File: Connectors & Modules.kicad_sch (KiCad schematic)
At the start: 1 part, among them M1 Xbee_MOdule

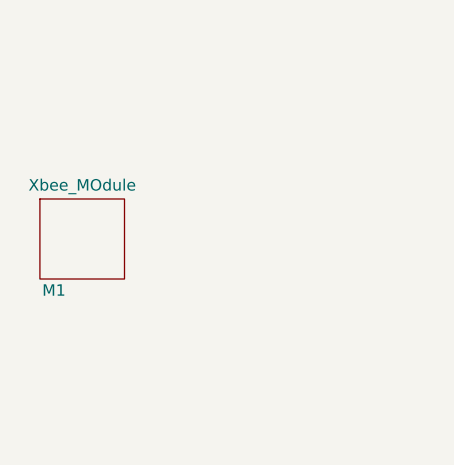
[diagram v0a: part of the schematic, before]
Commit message: Connectors Added
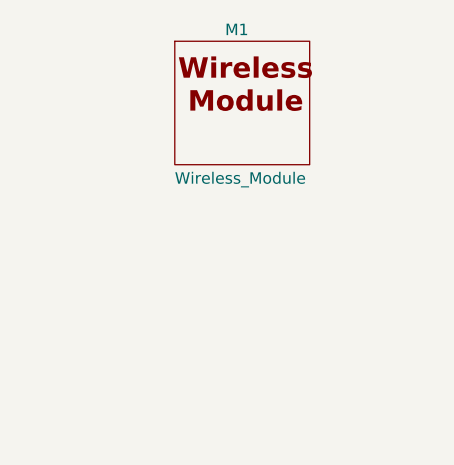
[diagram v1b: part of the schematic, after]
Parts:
- removed M1: Xbee_MOdule, LOGSUN:LGS-KC-Zbee_Mod, symbol LOGSUN:Xbee_MOD
- added M1: Wireless_Module, symbol LOGSUN:Wireless_MOD
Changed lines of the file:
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@@
+	)
+	(symbol
+		(lib_id "LOGSUN:Wireless_MOD")
+		(at 259.08 34.29 0)
+		(unit 1)
+		(exclude_from_sim no)
+		(in_bom yes)
+		(on_board yes)
+		(dnp no)
+		(property "Reference" "M1"
+			(at 258.572 24.892 0)
+			(effects
+				(font
+					(size 1.27 1.27)
+				)
+				(justify left)
+			)
+		)
+		(property "Value" "Wireless_Module"
+			(at 252.984 41.402 0)
+			(effects
+				(font
+					(size 1.27 1.27)
+				)
+				(justify left)
+			)
+		)
+		(property "Footprint" ""
+			(at 259.08 34.29 0)
+			(effects
+				(font
+					(size 1.27 1.27)
+				)
+				(hide yes)
+			)
+		)
+		(property "Datasheet" ""
+			(at 259.08 34.29 0)
+			(effects
+				(font
+					(size 1.27 1.27)
+				)
+				(hide yes)
+			)
+		)
+		(property "Description" ""
+			(at 259.08 34.29 0)
+			(effects
+				(font
+					(size 1.27 1.27)
+				)
+				(hide yes)
+			)
+		)
+		(instances
+			(project ""
+				(path "/99e6c4b3-8320-4218-aa5a-41657e7e07c6/0277d16f-7bc8-4de9-be5c-c06802e62271"
+					(reference "M1")
+					(unit 1)
+				)
+			)
+		)
 	)
 	(symbol
@@
 					(unit 1)
 				)
-			)
-		)
-	)
-	(symbol
-		(lib_id "LOGSUN:Xbee_MOD")
-		(at 241.3 46.99 0)
-		(unit 1)
-		(exclude_from_sim no)
-		(in_bom yes)
-		(on_board yes)
-		(dnp no)
-		(property "Reference" "M1"
-			(at 238.252 53.848 0)
-			(effects
-				(font
-					(size 1.27 1.27)
-				)
-				(justify left)
-			)
-		)
-		(property "Value" "Xbee_MOdule"
-			(at 236.728 42.164 0)
-			(effects
-				(font
-					(size 1.27 1.27)
-				)
-				(justify left)
-			)
-		)
-		(property "Footprint" "LOGSUN:LGS-KC-Zbee_Mod"
-			(at 241.3 46.99 0)
-			(effects
-				(font
-					(size 1.27 1.27)
-				)
-				(hide yes)
-			)
-		)
-		(property "Datasheet" ""
-			(at 241.3 46.99 0)
-			(effects
-				(font
-					(size 1.27 1.27)
-				)
-				(hide yes)
-			)
-		)
-		(property "Description" ""
-			(at 241.3 46.99 0)
-			(effects
-				(font
-					(size 1.27 1.27)
-				)
-				(hide yes)
-			)
-		)
-		(instances
-			(project ""
-				(path "/99e6c4b3-8320-4218-aa5a-41657e7e07c6/0277d16f-7bc8-4de9-be5c-c06802e62271"
-					(reference "M1")
-					(unit 1)
-				)

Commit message: Schematic Completed, Footprints Assigned
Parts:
- added J11, J12: Conn_01x03_Pin, Connector_JST:JST_EH_B3B-EH-A_1x03_P2.50mm_Vertical, symbol Connector:Conn_01x03_Pin
- added J13: I2C, Connector_JST:JST_EH_B4B-EH-A_1x04_P2.50mm_Vertical, symbol Connector:Conn_01x04_Pin
- added J14: UART, Connector_JST:JST_EH_B4B-EH-A_1x04_P2.50mm_Vertical, symbol Connector:Conn_01x04_Pin
- added J15: RGB, Connector_JST:JST_EH_B5B-EH-A_1x05_P2.50mm_Vertical, symbol Connector:Conn_01x05_Pin
- added J16: POT, Connector_JST:JST_EH_B5B-EH-A_1x05_P2.50mm_Vertical, symbol Connector:Conn_01x05_Pin
- added SV5: GP1, LOGSUN:LGS-KC-ML10-CONTROLLER, symbol LOGSUN:LGS-KC-ML10-CONTROLLER
- added SV6: GP2, LOGSUN:LGS-KC-ML10-CONTROLLER, symbol LOGSUN:LGS-KC-ML10-CONTROLLER
- added SV7: UEXT, LOGSUN:LGS-KC-ML10-CONTROLLER, symbol LOGSUN:LGS-KC-ML10-CONTROLLER
- M1: footprint (none) -> LOGSUN:LGS-KC-Wireless_Mod
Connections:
- new net +5V: J11.1 (Pin_1), J12.1 (Pin_1), J13.1 (Pin_1), J14.1 (Pin_1), SV5.1, SV6.1, SV7.1
- new net GND: J11.3 (Pin_3), J12.3 (Pin_3), J13.4 (Pin_4), J14.4 (Pin_4), SV5.2, SV6.2, SV7.2
- new net IO00: SV5.3
- new net IO02: SV5.5
- new net IO04: SV5.6
- new net IO05: SV7.10
- new net IO12: SV5.8
- new net IO13: SV5.7
- new net IO14: SV5.9
- new net IO15: SV5.4
- new net IO16: J14.3 (Pin_3), SV7.4
- new net IO17: J14.2 (Pin_2), SV7.3
- new net IO18: SV7.9
- new net IO19: SV7.7
- new net IO21: J13.3 (Pin_3), SV7.6
- new net IO22: J13.2 (Pin_2), SV7.5
- new net IO23: SV7.8
- new net IO25: SV6.9
- new net IO26: SV6.10
- new net IO27: SV5.10
- new net IO32: J12.2 (Pin_2), SV6.7
- new net IO33: J11.2 (Pin_2), SV6.8
- new net IO34: J16.4 (Pin_4), SV6.5
- new net IO35: SV6.6
- new net IO36: J16.3 (Pin_3), SV6.3
- new net IO39: J16.2 (Pin_2), SV6.4
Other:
- moved on the sheet: M1

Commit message: Bar LED Resistors Added & Mounting holes added
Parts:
- added H1, H2, H3, H4: MountingHole, MountingHole:MountingHole_3.2mm_M3_Pad_Via, symbol Mechanical:MountingHole

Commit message: Symbol and footprint library exported
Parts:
- H1, H2, H3, H4: symbol Mechanical:MountingHole -> ESP32_Xbee_LoRa:MountingHole
- J11, J12: symbol Connector:Conn_01x03_Pin -> ESP32_Xbee_LoRa:Conn_01x03_Pin
- J13, J14: symbol Connector:Conn_01x04_Pin -> ESP32_Xbee_LoRa:Conn_01x04_Pin
- J15, J16: symbol Connector:Conn_01x05_Pin -> ESP32_Xbee_LoRa:Conn_01x05_Pin
- M1: symbol LOGSUN:Wireless_MOD -> ESP32_Xbee_LoRa:Wireless_MOD
- SV5, SV6, SV7: symbol LOGSUN:LGS-KC-ML10-CONTROLLER -> ESP32_Xbee_LoRa:LGS-KC-ML10-CONTROLLER
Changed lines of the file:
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@@
 	)
 	(symbol
-		(lib_id "power:GND")
+		(lib_id "ESP32_Xbee_LoRa:GND")
 		(at 102.87 80.01 180)
 		(unit 1)
@@
 	)
 	(symbol
-		(lib_id "LOGSUN:LGS-KC-ML10-CONTROLLER")
+		(lib_id "ESP32_Xbee_LoRa:LGS-KC-ML10-CONTROLLER")
 		(at 93.98 127 180)
 		(unit 1)
@@
 	)
 	(symbol
-		(lib_id "Mechanical:MountingHole")
+		(lib_id "ESP32_Xbee_LoRa:MountingHole")
 		(at 165.1 88.9 0)
 		(unit 1)
@@
 	)
 	(symbol
-		(lib_id "power:+5V")
+		(lib_id "ESP32_Xbee_LoRa:+5V")
 		(at 274.32 25.4 0)
 		(unit 1)
@@
 	)
 	(symbol
-		(lib_id "power:+5V")
+		(lib_id "ESP32_Xbee_LoRa:+5V")
 		(at 236.22 55.88 0)
 		(unit 1)
@@
 	)
 	(symbol
-		(lib_id "Connector:Conn_01x03_Pin")
+		(lib_id "ESP32_Xbee_LoRa:Conn_01x03_Pin")
 		(at 264.16 30.48 0)
 		(unit 1)
@@
 	)
 	(symbol
-		(lib_id "power:GND")
+		(lib_id "ESP32_Xbee_LoRa:GND")
 		(at 274.32 35.56 0)
 		(unit 1)
@@
 	)
 	(symbol
-		(lib_id "power:+5V")
+		(lib_id "ESP32_Xbee_LoRa:+5V")
 		(at 236.22 25.4 0)
 		(unit 1)
@@
 	)
 	(symbol
-		(lib_id "power:+5V")
+		(lib_id "ESP32_Xbee_LoRa:+5V")
 		(at 85.09 80.01 0)
 		(unit 1)
@@
 	)
 	(symbol
-		(lib_id "Mechanical:MountingHole")
+		(lib_id "ESP32_Xbee_LoRa:MountingHole")
 		(at 162.56 74.93 0)
 		(unit 1)
@@
 	)
 	(symbol
-		(lib_id "LOGSUN:LGS-KC-ML10-CONTROLLER")
+		(lib_id "ESP32_Xbee_LoRa:LGS-KC-ML10-CONTROLLER")
 		(at 93.98 87.63 180)
 		(unit 1)
@@
 	)
 	(symbol
-		(lib_id "power:GND")
+		(lib_id "ESP32_Xbee_LoRa:GND")
 		(at 236.22 66.04 0)
 		(unit 1)
@@
 	)
 	(symbol
-		(lib_id "Connector:Conn_01x05_Pin")
+		(lib_id "ESP32_Xbee_LoRa:Conn_01x05_Pin")
 		(at 233.68 99.06 0)
 		(unit 1)
@@
 	)
 	(symbol
-		(lib_id "power:+5V")
+		(lib_id "ESP32_Xbee_LoRa:+5V")
 		(at 85.09 119.38 0)
 		(unit 1)
@@
 	)
 	(symbol
-		(lib_id "power:GND")
+		(lib_id "ESP32_Xbee_LoRa:GND")
 		(at 102.87 52.07 180)
 		(unit 1)
@@
 	)
 	(symbol
-		(lib_id "power:GND")
+		(lib_id "ESP32_Xbee_LoRa:GND")
 		(at 102.87 119.38 180)
 		(unit 1)
@@
 	)
 	(symbol
-		(lib_id "power:+5V")
+		(lib_id "ESP32_Xbee_LoRa:+5V")
 		(at 271.78 57.15 0)
 		(unit 1)
@@
 	)
 	(symbol
-		(lib_id "LOGSUN:Wireless_MOD")
+		(lib_id "ESP32_Xbee_LoRa:Wireless_MOD")
 		(at 41.91 34.29 0)
 		(unit 1)
@@
 	)
 	(symbol
-		(lib_id "power:GND")
+		(lib_id "ESP32_Xbee_LoRa:GND")
 		(at 271.78 67.31 0)
 		(unit 1)
@@
 	)
 	(symbol
-		(lib_id "Connector:Conn_01x04_Pin")
+		(lib_id "ESP32_Xbee_LoRa:Conn_01x04_Pin")
 		(at 227.33 59.69 0)
 		(unit 1)
@@
 	)
 	(symbol
-		(lib_id "power:GND")
+		(lib_id "ESP32_Xbee_LoRa:GND")
 		(at 236.22 35.56 0)
 		(unit 1)
@@
 	)
 	(symbol
-		(lib_id "power:+5V")
+		(lib_id "ESP32_Xbee_LoRa:+5V")
 		(at 85.09 52.07 0)
 		(unit 1)
@@
 	)
 	(symbol
-		(lib_id "LOGSUN:LGS-KC-ML10-CONTROLLER")
+		(lib_id "ESP32_Xbee_LoRa:LGS-KC-ML10-CONTROLLER")
 		(at 93.98 60.96 180)
 		(unit 1)
@@
 	)
 	(symbol
-		(lib_id "Connector:Conn_01x04_Pin")
+		(lib_id "ESP32_Xbee_LoRa:Conn_01x04_Pin")
 		(at 264.16 60.96 0)
 		(unit 1)
@@
 	)
 	(symbol
-		(lib_id "Connector:Conn_01x05_Pin")
+		(lib_id "ESP32_Xbee_LoRa:Conn_01x05_Pin")
 		(at 259.08 100.33 0)
 		(unit 1)
@@
 	)
 	(symbol
-		(lib_id "Connector:Conn_01x03_Pin")
+		(lib_id "ESP32_Xbee_LoRa:Conn_01x03_Pin")
 		(at 226.06 30.48 0)
 		(unit 1)
@@
 	)
 	(symbol
-		(lib_id "Logsun_Logo:LOGO")
+		(lib_id "ESP32_Xbee_LoRa:LOGO")
 		(at 259.08 173.99 0)
 		(unit 1)
@@
 	)
 	(symbol
-		(lib_id "Mechanical:MountingHole")
+		(lib_id "ESP32_Xbee_LoRa:MountingHole")
 		(at 170.18 102.87 0)
 		(unit 1)
@@
 	)
 	(symbol
-		(lib_id "Mechanical:MountingHole")
+		(lib_id "ESP32_Xbee_LoRa:MountingHole")
 		(at 163.83 63.5 0)
 		(unit 1)
